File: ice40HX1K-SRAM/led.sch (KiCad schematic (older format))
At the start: 40 parts

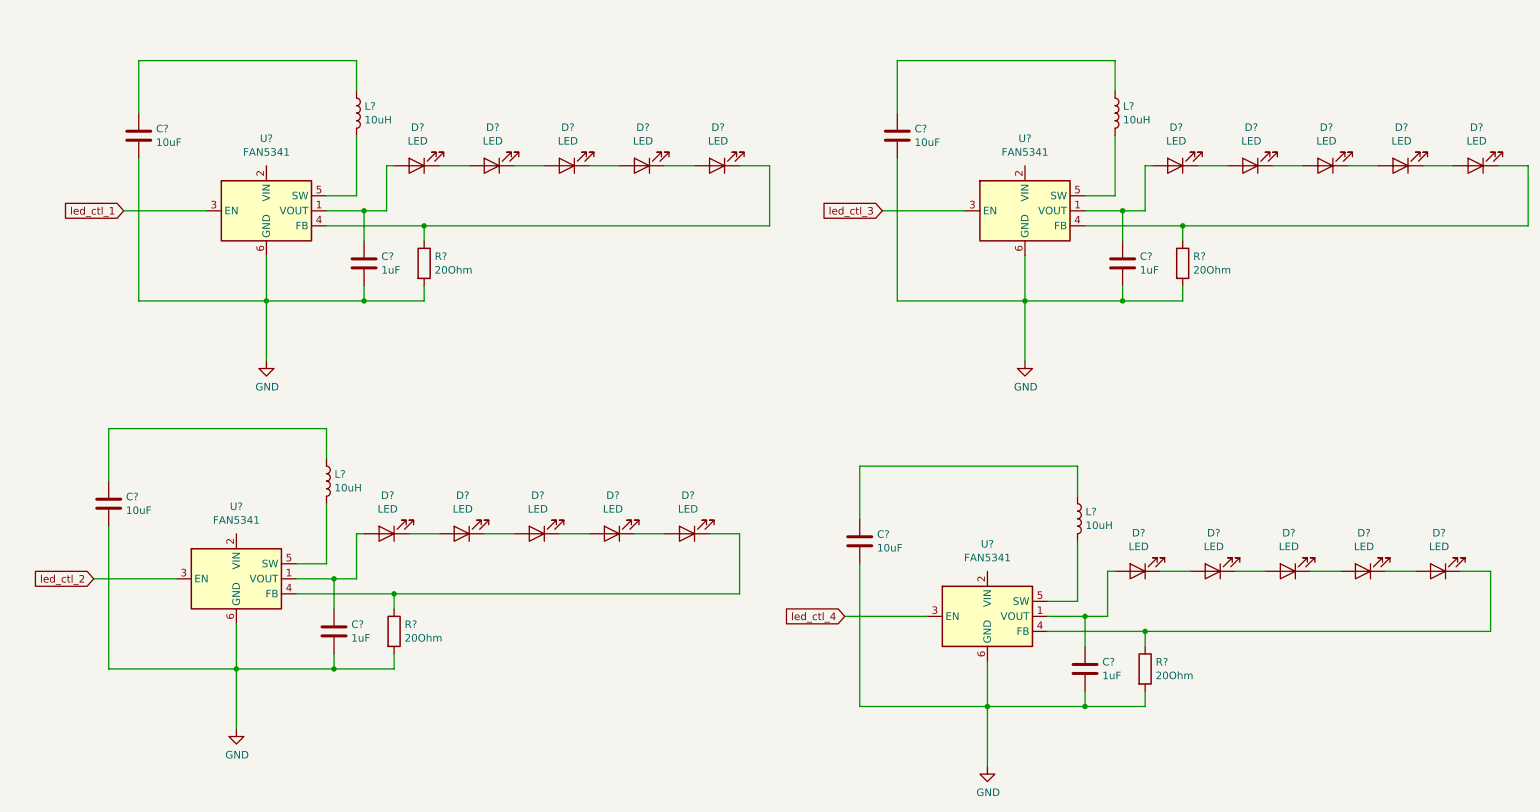
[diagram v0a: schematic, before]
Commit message: wiring FPGA nRF52 and ATSAMD11
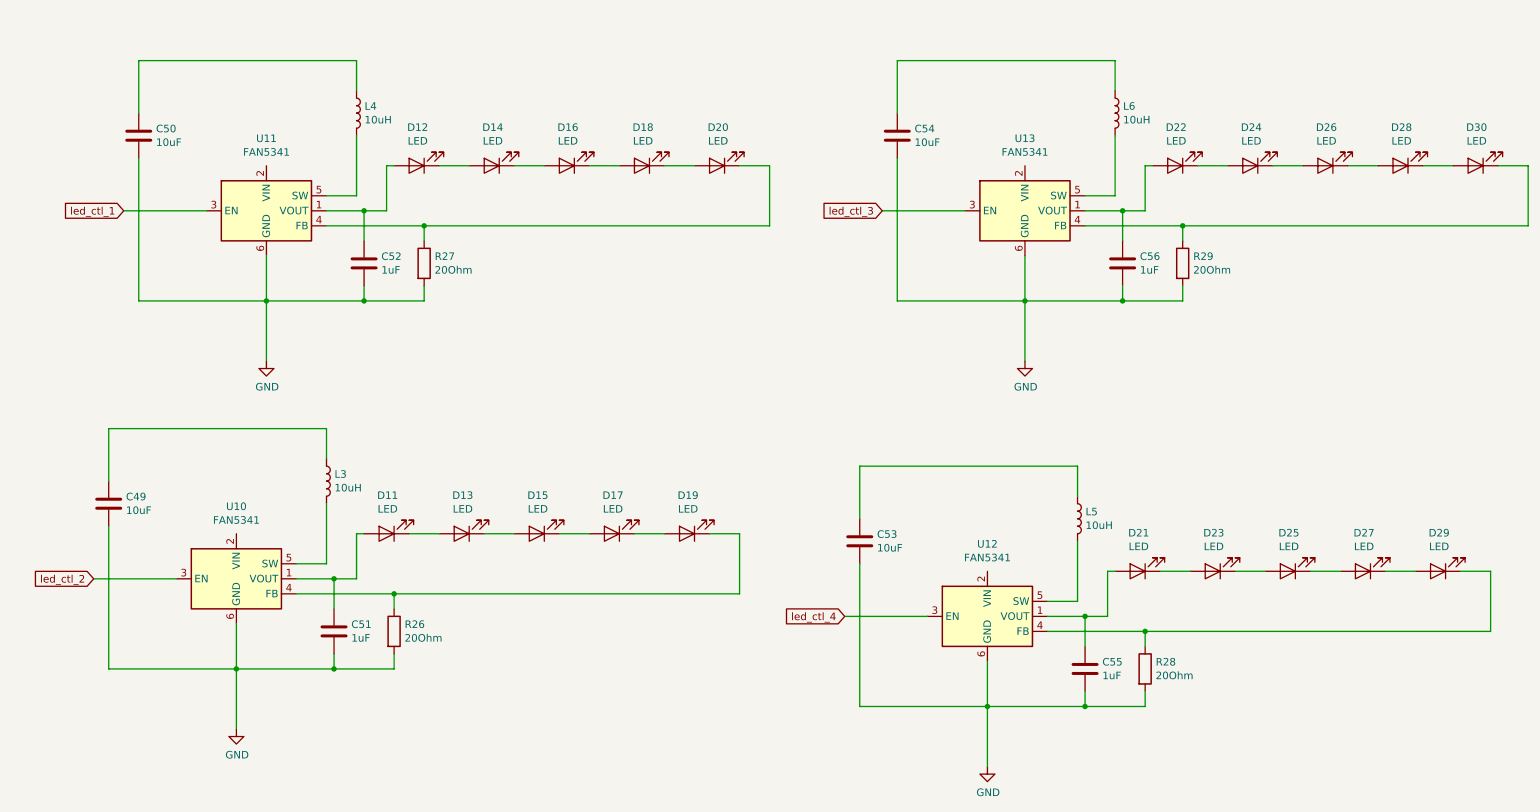
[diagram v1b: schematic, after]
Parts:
- gave numbers to parts that had none: 40

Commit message: wiring FPGA
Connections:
- net +3V3: now reaches U11.2 (VIN)
- net +3V3: now also C49.1, C50.1, C53.1, C54.1, L3.1, L4.1, L5.1, L6.1, U10.2 (VIN), U12.2 (VIN), U13.2 (VIN)
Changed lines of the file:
@@
 	1350 1300 1350 950
 Wire Wire Line
-	1350 950  2800 950
+	1350 950  2200 950
 Wire Wire Line
 	2800 950  2800 1150
@@
 	1150 3750 1150 3400
 Wire Wire Line
-	1150 3400 2600 3400
+	1150 3400 2000 3400
 Wire Wire Line
 	2600 3400 2600 3600
@@
 	6400 1300 6400 950
 Wire Wire Line
-	6400 950  7850 950
+	6400 950  7250 950
 Wire Wire Line
 	7850 950  7850 1150
@@
 	6150 4000 6150 3650
 Wire Wire Line
-	6150 3650 7600 3650
+	6150 3650 7000 3650
 Wire Wire Line
 	7600 3650 7600 3850
@@
 	10350 4750 8050 4750
 Connection ~ 8050 4750
+$Comp
+L power:+3V3 #PWR0100
+U 1 1 5E715360
+P 2000 3300
+F 0 "#PWR0100" H 2000 3150 50  0001 C CNN
+F 1 "+3V3" H 2015 3473 50  0000 C CNN
+F 2 "" H 2000 3300 50  0001 C CNN
+F 3 "" H 2000 3300 50  0001 C CNN
+	1    2000 3300
+	1    0    0    -1
+$EndComp
+Wire Wire Line
+	2000 3300 2000 3400
+Connection ~ 2000 3400
+Wire Wire Line
+	2000 3400 2600 3400
+Wire Wire Line
+	2000 4100 2000 3400
+$Comp
+L power:+3V3 #PWR0102
+U 1 1 5E71F28F
+P 2200 850
+F 0 "#PWR0102" H 2200 700 50  0001 C CNN
+F 1 "+3V3" H 2215 1023 50  0000 C CNN
+F 2 "" H 2200 850 50  0001 C CNN
+F 3 "" H 2200 850 50  0001 C CNN
+	1    2200 850
+	1    0    0    -1
+$EndComp
+Wire Wire Line
+	2200 850  2200 950
+Connection ~ 2200 950
+Wire Wire Line
+	2200 950  2800 950
+Wire Wire Line
+	2200 1650 2200 950
+$Comp
+L power:+3V3 #PWR0104
+U 1 1 5E72402D
+P 7250 850
+F 0 "#PWR0104" H 7250 700 50  0001 C CNN
+F 1 "+3V3" H 7265 1023 50  0000 C CNN
+F 2 "" H 7250 850 50  0001 C CNN
+F 3 "" H 7250 850 50  0001 C CNN
+	1    7250 850
+	1    0    0    -1
+$EndComp
+Wire Wire Line
+	7250 850  7250 950
+Connection ~ 7250 950
+Wire Wire Line
+	7250 950  7850 950
+Wire Wire Line
+	7250 1650 7250 950
+$Comp
+L power:+3V3 #PWR0103
+U 1 1 5E729610
+P 7000 3550
+F 0 "#PWR0103" H 7000 3400 50  0001 C CNN
+F 1 "+3V3" H 7015 3723 50  0000 C CNN
+F 2 "" H 7000 3550 50  0001 C CNN
+F 3 "" H 7000 3550 50  0001 C CNN
+	1    7000 3550
+	1    0    0    -1
+$EndComp
+Wire Wire Line
+	7000 3550 7000 3650
+Connection ~ 7000 3650
+Wire Wire Line
+	7000 3650 7600 3650
+Wire Wire Line
+	7000 4350 7000 3650
 $EndSCHEMATC

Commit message: wiring FPGA
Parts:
- R26, R27, R28, R29: footprint (none) -> Resistor_SMD:R_0402_1005Metric
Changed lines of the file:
@@
 F 0 "R27" H 3320 2346 50  0000 L CNN
 F 1 "20Ohm" H 3320 2255 50  0000 L CNN
-F 2 "" V 3180 2300 50  0001 C CNN
+F 2 "Resistor_SMD:R_0402_1005Metric" V 3180 2300 50  0001 C CNN
 F 3 "~" H 3250 2300 50  0001 C CNN
 	1    3250 2300
@@
 F 0 "R26" H 3120 4796 50  0000 L CNN
 F 1 "20Ohm" H 3120 4705 50  0000 L CNN
-F 2 "" V 2980 4750 50  0001 C CNN
+F 2 "Resistor_SMD:R_0402_1005Metric" V 2980 4750 50  0001 C CNN
 F 3 "~" H 3050 4750 50  0001 C CNN
 	1    3050 4750
@@
 F 0 "R29" H 8370 2346 50  0000 L CNN
 F 1 "20Ohm" H 8370 2255 50  0000 L CNN
-F 2 "" V 8230 2300 50  0001 C CNN
+F 2 "Resistor_SMD:R_0402_1005Metric" V 8230 2300 50  0001 C CNN
 F 3 "~" H 8300 2300 50  0001 C CNN
 	1    8300 2300
@@
 F 0 "R28" H 8120 5046 50  0000 L CNN
 F 1 "20Ohm" H 8120 4955 50  0000 L CNN
-F 2 "" V 7980 5000 50  0001 C CNN
+F 2 "Resistor_SMD:R_0402_1005Metric" V 7980 5000 50  0001 C CNN
 F 3 "~" H 8050 5000 50  0001 C CNN
 	1    8050 5000

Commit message: starting layout
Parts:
- C49, C50, C53, C54: footprint (none) -> Capacitor_SMD:C_0603_1608Metric
- C51, C52, C55, C56: footprint (none) -> Capacitor_SMD:C_0402_1005Metric
- D11, D12, D13, D14, D15, D16, D17, D18, D19, D20, D21, D22, D23, D24, D25, D26, D27, D28, D29, D30: footprint (none) -> LED_SMD:LED_1206_3216Metric
- L3, L4, L5, L6: footprint (none) -> Inductor_SMD:L_0805_2012Metric
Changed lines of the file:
@@
 F 0 "C50" H 1465 1496 50  0000 L CNN
 F 1 "10uF" H 1465 1405 50  0000 L CNN
-F 2 "" H 1388 1300 50  0001 C CNN
+F 2 "Capacitor_SMD:C_0603_1608Metric" H 1388 1300 50  0001 C CNN
 F 3 "~" H 1350 1450 50  0001 C CNN
 	1    1350 1450
@@
 F 0 "L4" H 2853 1346 50  0000 L CNN
 F 1 "10uH" H 2853 1255 50  0000 L CNN
-F 2 "" H 2800 1300 50  0001 C CNN
+F 2 "Inductor_SMD:L_0805_2012Metric" H 2800 1300 50  0001 C CNN
 F 3 "~" H 2800 1300 50  0001 C CNN
 	1    2800 1300
@@
 F 0 "C52" H 2965 2346 50  0000 L CNN
 F 1 "1uF" H 2965 2255 50  0000 L CNN
-F 2 "" H 2888 2150 50  0001 C CNN
+F 2 "Capacitor_SMD:C_0402_1005Metric" H 2888 2150 50  0001 C CNN
 F 3 "~" H 2850 2300 50  0001 C CNN
 	1    2850 2300
@@
 F 0 "D12" H 3193 1395 50  0000 C CNN
 F 1 "LED" H 3193 1486 50  0000 C CNN
-F 2 "" H 3200 1650 50  0001 C CNN
+F 2 "LED_SMD:LED_1206_3216Metric" H 3200 1650 50  0001 C CNN
 F 3 "~" H 3200 1650 50  0001 C CNN
 	1    3200 1650
@@
 F 0 "D14" H 3693 1395 50  0000 C CNN
 F 1 "LED" H 3693 1486 50  0000 C CNN
-F 2 "" H 3700 1650 50  0001 C CNN
+F 2 "LED_SMD:LED_1206_3216Metric" H 3700 1650 50  0001 C CNN
 F 3 "~" H 3700 1650 50  0001 C CNN
 	1    3700 1650
@@
 F 0 "D16" H 4193 1395 50  0000 C CNN
 F 1 "LED" H 4193 1486 50  0000 C CNN
-F 2 "" H 4200 1650 50  0001 C CNN
+F 2 "LED_SMD:LED_1206_3216Metric" H 4200 1650 50  0001 C CNN
 F 3 "~" H 4200 1650 50  0001 C CNN
 	1    4200 1650
@@
 F 0 "D18" H 4693 1395 50  0000 C CNN
 F 1 "LED" H 4693 1486 50  0000 C CNN
-F 2 "" H 4700 1650 50  0001 C CNN
+F 2 "LED_SMD:LED_1206_3216Metric" H 4700 1650 50  0001 C CNN
 F 3 "~" H 4700 1650 50  0001 C CNN
 	1    4700 1650
@@
 F 0 "D20" H 5193 1395 50  0000 C CNN
 F 1 "LED" H 5193 1486 50  0000 C CNN
-F 2 "" H 5200 1650 50  0001 C CNN
+F 2 "LED_SMD:LED_1206_3216Metric" H 5200 1650 50  0001 C CNN
 F 3 "~" H 5200 1650 50  0001 C CNN
 	1    5200 1650
@@
 F 0 "C49" H 1265 3946 50  0000 L CNN
 F 1 "10uF" H 1265 3855 50  0000 L CNN
-F 2 "" H 1188 3750 50  0001 C CNN
+F 2 "Capacitor_SMD:C_0603_1608Metric" H 1188 3750 50  0001 C CNN
 F 3 "~" H 1150 3900 50  0001 C CNN
 	1    1150 3900
@@
 F 0 "L3" H 2653 3796 50  0000 L CNN
 F 1 "10uH" H 2653 3705 50  0000 L CNN
-F 2 "" H 2600 3750 50  0001 C CNN
+F 2 "Inductor_SMD:L_0805_2012Metric" H 2600 3750 50  0001 C CNN
 F 3 "~" H 2600 3750 50  0001 C CNN
 	1    2600 3750
@@
 F 0 "C51" H 2765 4796 50  0000 L CNN
 F 1 "1uF" H 2765 4705 50  0000 L CNN
-F 2 "" H 2688 4600 50  0001 C CNN
+F 2 "Capacitor_SMD:C_0402_1005Metric" H 2688 4600 50  0001 C CNN
 F 3 "~" H 2650 4750 50  0001 C CNN
 	1    2650 4750
@@
 F 0 "D11" H 2993 3845 50  0000 C CNN
 F 1 "LED" H 2993 3936 50  0000 C CNN
-F 2 "" H 3000 4100 50  0001 C CNN
+F 2 "LED_SMD:LED_1206_3216Metric" H 3000 4100 50  0001 C CNN
 F 3 "~" H 3000 4100 50  0001 C CNN
 	1    3000 4100
@@
 F 0 "D13" H 3493 3845 50  0000 C CNN
 F 1 "LED" H 3493 3936 50  0000 C CNN
-F 2 "" H 3500 4100 50  0001 C CNN
+F 2 "LED_SMD:LED_1206_3216Metric" H 3500 4100 50  0001 C CNN
 F 3 "~" H 3500 4100 50  0001 C CNN
 	1    3500 4100
@@
 F 0 "D15" H 3993 3845 50  0000 C CNN
 F 1 "LED" H 3993 3936 50  0000 C CNN
-F 2 "" H 4000 4100 50  0001 C CNN
+F 2 "LED_SMD:LED_1206_3216Metric" H 4000 4100 50  0001 C CNN
 F 3 "~" H 4000 4100 50  0001 C CNN
 	1    4000 4100
@@
 F 0 "D17" H 4493 3845 50  0000 C CNN
 F 1 "LED" H 4493 3936 50  0000 C CNN
-F 2 "" H 4500 4100 50  0001 C CNN
+F 2 "LED_SMD:LED_1206_3216Metric" H 4500 4100 50  0001 C CNN
 F 3 "~" H 4500 4100 50  0001 C CNN
 	1    4500 4100
@@
 F 0 "D19" H 4993 3845 50  0000 C CNN
 F 1 "LED" H 4993 3936 50  0000 C CNN
-F 2 "" H 5000 4100 50  0001 C CNN
+F 2 "LED_SMD:LED_1206_3216Metric" H 5000 4100 50  0001 C CNN
 F 3 "~" H 5000 4100 50  0001 C CNN
 	1    5000 4100
@@
 F 0 "C54" H 6515 1496 50  0000 L CNN
 F 1 "10uF" H 6515 1405 50  0000 L CNN
-F 2 "" H 6438 1300 50  0001 C CNN
+F 2 "Capacitor_SMD:C_0603_1608Metric" H 6438 1300 50  0001 C CNN
 F 3 "~" H 6400 1450 50  0001 C CNN
 	1    6400 1450
@@
 F 0 "L6" H 7903 1346 50  0000 L CNN
 F 1 "10uH" H 7903 1255 50  0000 L CNN
-F 2 "" H 7850 1300 50  0001 C CNN
+F 2 "Inductor_SMD:L_0805_2012Metric" H 7850 1300 50  0001 C CNN
 F 3 "~" H 7850 1300 50  0001 C CNN
 	1    7850 1300
@@
 F 0 "C56" H 8015 2346 50  0000 L CNN
 F 1 "1uF" H 8015 2255 50  0000 L CNN
-F 2 "" H 7938 2150 50  0001 C CNN
+F 2 "Capacitor_SMD:C_0402_1005Metric" H 7938 2150 50  0001 C CNN
 F 3 "~" H 7900 2300 50  0001 C CNN
 	1    7900 2300
@@
 F 0 "D22" H 8243 1395 50  0000 C CNN
 F 1 "LED" H 8243 1486 50  0000 C CNN
-F 2 "" H 8250 1650 50  0001 C CNN
+F 2 "LED_SMD:LED_1206_3216Metric" H 8250 1650 50  0001 C CNN
 F 3 "~" H 8250 1650 50  0001 C CNN
 	1    8250 1650
@@
 F 0 "D24" H 8743 1395 50  0000 C CNN
 F 1 "LED" H 8743 1486 50  0000 C CNN
-F 2 "" H 8750 1650 50  0001 C CNN
+F 2 "LED_SMD:LED_1206_3216Metric" H 8750 1650 50  0001 C CNN
 F 3 "~" H 8750 1650 50  0001 C CNN
 	1    8750 1650
@@
 F 0 "D26" H 9243 1395 50  0000 C CNN
 F 1 "LED" H 9243 1486 50  0000 C CNN
-F 2 "" H 9250 1650 50  0001 C CNN
+F 2 "LED_SMD:LED_1206_3216Metric" H 9250 1650 50  0001 C CNN
 F 3 "~" H 9250 1650 50  0001 C CNN
 	1    9250 1650
@@
 F 0 "D28" H 9743 1395 50  0000 C CNN
 F 1 "LED" H 9743 1486 50  0000 C CNN
-F 2 "" H 9750 1650 50  0001 C CNN
+F 2 "LED_SMD:LED_1206_3216Metric" H 9750 1650 50  0001 C CNN
 F 3 "~" H 9750 1650 50  0001 C CNN
 	1    9750 1650
@@
 F 0 "D30" H 10243 1395 50  0000 C CNN
 F 1 "LED" H 10243 1486 50  0000 C CNN
-F 2 "" H 10250 1650 50  0001 C CNN
+F 2 "LED_SMD:LED_1206_3216Metric" H 10250 1650 50  0001 C CNN
 F 3 "~" H 10250 1650 50  0001 C CNN
 	1    10250 1650
@@
 F 0 "C53" H 6265 4196 50  0000 L CNN
 F 1 "10uF" H 6265 4105 50  0000 L CNN
-F 2 "" H 6188 4000 50  0001 C CNN
+F 2 "Capacitor_SMD:C_0603_1608Metric" H 6188 4000 50  0001 C CNN
 F 3 "~" H 6150 4150 50  0001 C CNN
 	1    6150 4150
@@
 F 0 "L5" H 7653 4046 50  0000 L CNN
 F 1 "10uH" H 7653 3955 50  0000 L CNN
-F 2 "" H 7600 4000 50  0001 C CNN
+F 2 "Inductor_SMD:L_0805_2012Metric" H 7600 4000 50  0001 C CNN
 F 3 "~" H 7600 4000 50  0001 C CNN
 	1    7600 4000
@@
 F 0 "C55" H 7765 5046 50  0000 L CNN
 F 1 "1uF" H 7765 4955 50  0000 L CNN
-F 2 "" H 7688 4850 50  0001 C CNN
+F 2 "Capacitor_SMD:C_0402_1005Metric" H 7688 4850 50  0001 C CNN
 F 3 "~" H 7650 5000 50  0001 C CNN
 	1    7650 5000
@@
 F 0 "D21" H 7993 4095 50  0000 C CNN
 F 1 "LED" H 7993 4186 50  0000 C CNN
-F 2 "" H 8000 4350 50  0001 C CNN
+F 2 "LED_SMD:LED_1206_3216Metric" H 8000 4350 50  0001 C CNN
 F 3 "~" H 8000 4350 50  0001 C CNN
 	1    8000 4350
@@
 F 0 "D23" H 8493 4095 50  0000 C CNN
 F 1 "LED" H 8493 4186 50  0000 C CNN
-F 2 "" H 8500 4350 50  0001 C CNN
+F 2 "LED_SMD:LED_1206_3216Metric" H 8500 4350 50  0001 C CNN
 F 3 "~" H 8500 4350 50  0001 C CNN
 	1    8500 4350
@@
 F 0 "D25" H 8993 4095 50  0000 C CNN
 F 1 "LED" H 8993 4186 50  0000 C CNN
-F 2 "" H 9000 4350 50  0001 C CNN
+F 2 "LED_SMD:LED_1206_3216Metric" H 9000 4350 50  0001 C CNN
 F 3 "~" H 9000 4350 50  0001 C CNN
 	1    9000 4350
@@
 F 0 "D27" H 9493 4095 50  0000 C CNN
 F 1 "LED" H 9493 4186 50  0000 C CNN
-F 2 "" H 9500 4350 50  0001 C CNN
+F 2 "LED_SMD:LED_1206_3216Metric" H 9500 4350 50  0001 C CNN
 F 3 "~" H 9500 4350 50  0001 C CNN
 	1    9500 4350
@@
 F 0 "D29" H 9993 4095 50  0000 C CNN
 F 1 "LED" H 9993 4186 50  0000 C CNN
-F 2 "" H 10000 4350 50  0001 C CNN
+F 2 "LED_SMD:LED_1206_3216Metric" H 10000 4350 50  0001 C CNN
 F 3 "~" H 10000 4350 50  0001 C CNN
 	1    10000 4350
